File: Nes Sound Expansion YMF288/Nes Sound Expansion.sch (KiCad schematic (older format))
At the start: 44 parts, among them J1 NES-SNES Port1, J2 NES-SNES Port2, J3 EXP 1-24, J4 EXP 25-48, J5 EN Switch, J6 AudioJack2_Ground_Switch, J7 EN LED, U1 74HC139D, U10 74HC257D, U2 74HC132D, U6 74HC174D, U7 74HC174D, U8 74HC257D, U9 74HC257D, X1 CXO_DIP8

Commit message: Added amplification for both famicom and nes model
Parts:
- removed C12, C13: 10uF, Capacitor_SMD:CP_Elec_4x5.3, symbol Device:CP
- removed R1, R2, R3: 1k, Resistor_SMD:R_0805_2012Metric, symbol Device:R
- added C12, C13, C6, C7: 10uF, Capacitor_SMD:C_0805_2012Metric, symbol Device:C
- added C8, C9: 68pF, Capacitor_SMD:C_0805_2012Metric, symbol Device:C
- added R20, R21, R22, R23, R26, R27: 47k, Resistor_SMD:R_0805_2012Metric, symbol Device:R
- added R24, R25: 3k, Resistor_SMD:R_0805_2012Metric, symbol Device:R
- added U3: LM358, Package_SO:SOIC-8_3.9x4.9mm_P1.27mm, symbol Amplifier_Operational:OPA2134
- C2: footprint Capacitor_SMD:CP_Elec_4x5.3 -> Capacitor_SMD:C_0805_2012Metric; symbol Device:CP -> Device:C
- R10: value 1k -> 10k
- X1: footprint Oscillator:Oscillator_SMD_SeikoEpson_SG8002CE-4Pin_3.2x2.5mm -> Oscillator:Oscillator_SMD_SeikoEpson_SG8002LB-4Pin_5.0x3.2mm
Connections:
- wire segments 118 -> 139
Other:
- moved on the sheet: C10, C11, R10, R5, R6, R7, R8, U10, U8, U9

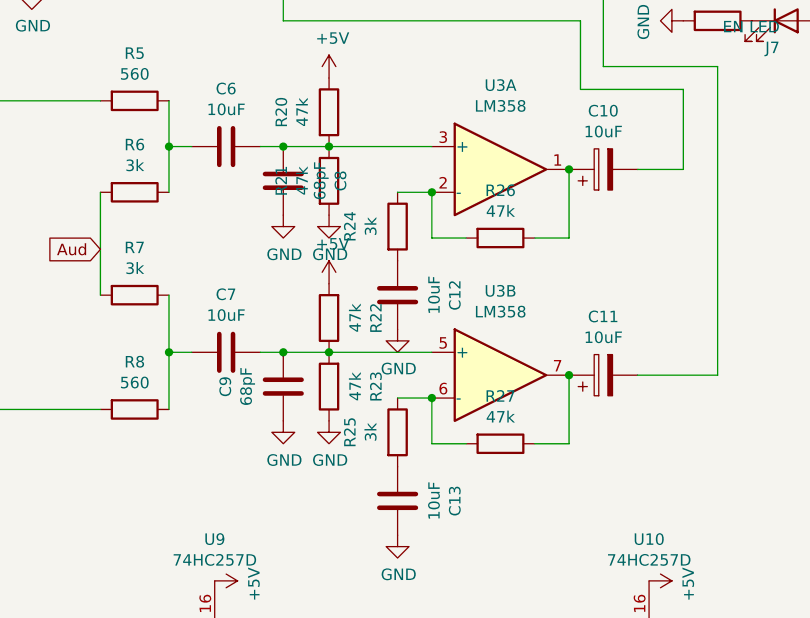
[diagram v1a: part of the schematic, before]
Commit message: Updated 401C-F addressing circuit
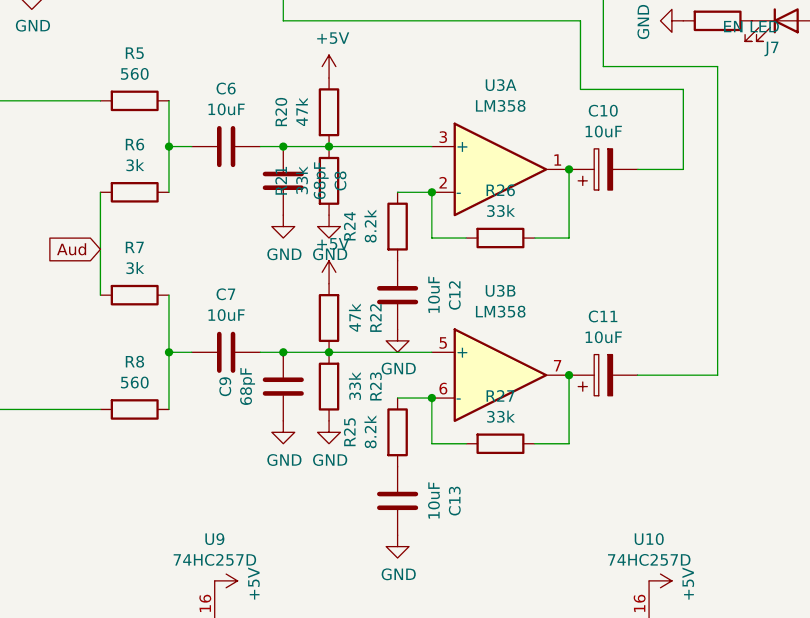
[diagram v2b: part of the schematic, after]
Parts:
- R21, R23, R26, R27: value 47k -> 33k
- R24, R25: value 3k -> 8.2k
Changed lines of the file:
@@
 P 9500 4000
 F 0 "R27" V 9293 4000 50  0000 C CNN
-F 1 "47k" V 9384 4000 50  0000 C CNN
+F 1 "33k" V 9384 4000 50  0000 C CNN
 F 2 "Resistor_SMD:R_0805_2012Metric" V 9430 4000 50  0001 C CNN
 F 3 "~" H 9500 4000 50  0001 C CNN
@@
 P 9050 3950
 F 0 "R25" V 8843 3950 50  0000 C CNN
-F 1 "3k" V 8934 3950 50  0000 C CNN
+F 1 "8.2k" V 8934 3950 50  0000 C CNN
 F 2 "Resistor_SMD:R_0805_2012Metric" V 8980 3950 50  0001 C CNN
 F 3 "~" H 9050 3950 50  0001 C CNN
@@
 P 8750 3750
 F 0 "R23" V 8543 3750 50  0000 C CNN
-F 1 "47k" V 8634 3750 50  0000 C CNN
+F 1 "33k" V 8634 3750 50  0000 C CNN
 F 2 "Resistor_SMD:R_0805_2012Metric" V 8680 3750 50  0001 C CNN
 F 3 "~" H 8750 3750 50  0001 C CNN
@@
 P 9500 3100
 F 0 "R26" V 9293 3100 50  0000 C CNN
-F 1 "47k" V 9384 3100 50  0000 C CNN
+F 1 "33k" V 9384 3100 50  0000 C CNN
 F 2 "Resistor_SMD:R_0805_2012Metric" V 9430 3100 50  0001 C CNN
 F 3 "~" H 9500 3100 50  0001 C CNN
@@
 P 9050 3050
 F 0 "R24" V 8843 3050 50  0000 C CNN
-F 1 "3k" V 8934 3050 50  0000 C CNN
+F 1 "8.2k" V 8934 3050 50  0000 C CNN
 F 2 "Resistor_SMD:R_0805_2012Metric" V 8980 3050 50  0001 C CNN
 F 3 "~" H 9050 3050 50  0001 C CNN
@@
 P 8750 2850
 F 0 "R21" V 8543 2850 50  0000 C CNN
-F 1 "47k" V 8634 2850 50  0000 C CNN
+F 1 "33k" V 8634 2850 50  0000 C CNN
 F 2 "Resistor_SMD:R_0805_2012Metric" V 8680 2850 50  0001 C CNN
 F 3 "~" H 8750 2850 50  0001 C CNN

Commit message: Removed power switch and updated resistor values
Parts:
- removed J5: EN Switch, Button_Switch_SMD:SW_DIP_SPSTx01_Slide_6.7x4.1mm_W6.73mm_P2.54mm_LowProfile_JPin, symbol Switch:SW_SPST
- R13: value 1k -> 3k
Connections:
- wire segments 139 -> 138
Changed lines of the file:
@@
 $EndComp
-Wire Wire Line
-	10600 1850 10500 1850
 Wire Wire Line
 	10500 1850 10500 2050
@@
 P 3600 6050
 F 0 "R13" V 3393 6050 50  0000 C CNN
-F 1 "1k" V 3484 6050 50  0000 C CNN
+F 1 "3k" V 3484 6050 50  0000 C CNN
 F 2 "Resistor_SMD:R_0805_2012Metric" V 3530 6050 50  0001 C CNN
 F 3 "~" H 3600 6050 50  0001 C CNN
@@
 	10500 2050 10900 2050
 $Comp
-L Switch:SW_SPST J5
-U 1 1 5F6BC120
-P 10800 1850
-F 0 "J5" H 10772 1732 50  0000 R CNN
-F 1 "EN Switch" H 10772 1823 50  0000 R CNN
-F 2 "Button_Switch_SMD:SW_DIP_SPSTx01_Slide_6.7x4.1mm_W6.73mm_P2.54mm_LowProfile_JPin" H 10800 1850 50  0001 C CNN
-F 3 "~" H 10800 1850 50  0001 C CNN
-	1    10800 1850
-	-1   0    0    1
-$EndComp
-Wire Wire Line
-	10600 1750 11000 1750
-Wire Wire Line
-	11000 1750 11000 1850
-$Comp
 L Device:C C4
 U 1 1 60444BC0
@@
 	1    0    0    -1
 $EndComp
+Wire Wire Line
+	10600 1750 10500 1750
+Wire Wire Line
+	10500 1750 10500 1850
 $EndSCHEMATC

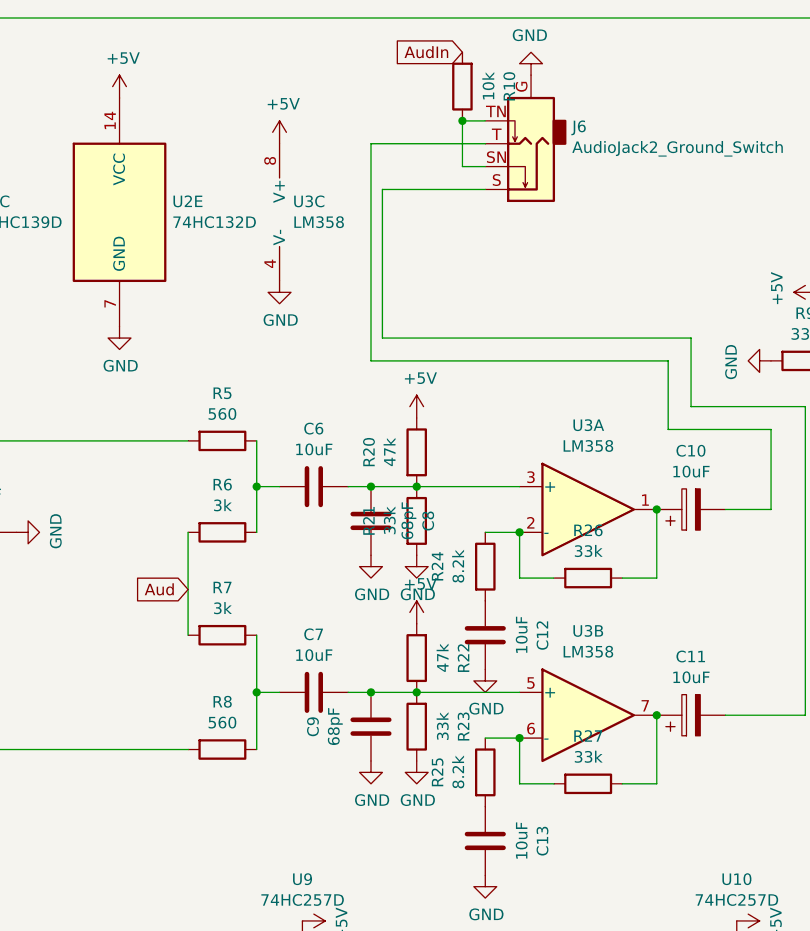
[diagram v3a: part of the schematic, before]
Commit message: Forgot to press save after editing resistor values
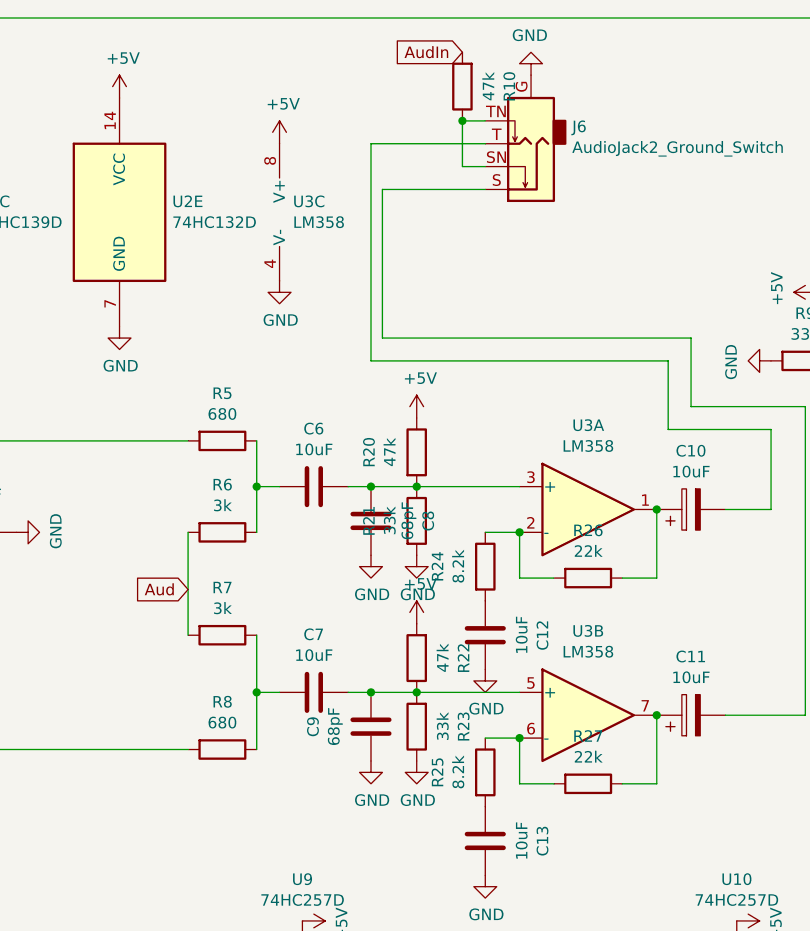
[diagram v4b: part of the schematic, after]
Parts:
- R10: value 10k -> 47k
- R26, R27: value 33k -> 22k
- R5, R8: value 560 -> 680
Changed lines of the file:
@@
 P 7900 2500
 F 0 "R5" V 7693 2500 50  0000 C CNN
-F 1 "560" V 7784 2500 50  0000 C CNN
+F 1 "680" V 7784 2500 50  0000 C CNN
 F 2 "Resistor_SMD:R_0805_2012Metric" V 7830 2500 50  0001 C CNN
 F 3 "~" H 7900 2500 50  0001 C CNN
@@
 P 7900 3850
 F 0 "R8" V 7693 3850 50  0000 C CNN
-F 1 "560" V 7784 3850 50  0000 C CNN
+F 1 "680" V 7784 3850 50  0000 C CNN
 F 2 "Resistor_SMD:R_0805_2012Metric" V 7830 3850 50  0001 C CNN
 F 3 "~" H 7900 3850 50  0001 C CNN
@@
 P 8950 950
 F 0 "R10" V 8743 950 50  0000 C CNN
-F 1 "10k" V 8834 950 50  0000 C CNN
+F 1 "47k" V 8834 950 50  0000 C CNN
 F 2 "Resistor_SMD:R_0805_2012Metric" V 8880 950 50  0001 C CNN
 F 3 "~" H 8950 950 50  0001 C CNN
@@
 P 9500 4000
 F 0 "R27" V 9293 4000 50  0000 C CNN
-F 1 "33k" V 9384 4000 50  0000 C CNN
+F 1 "22k" V 9384 4000 50  0000 C CNN
 F 2 "Resistor_SMD:R_0805_2012Metric" V 9430 4000 50  0001 C CNN
 F 3 "~" H 9500 4000 50  0001 C CNN
@@
 P 9500 3100
 F 0 "R26" V 9293 3100 50  0000 C CNN
-F 1 "33k" V 9384 3100 50  0000 C CNN
+F 1 "22k" V 9384 3100 50  0000 C CNN
 F 2 "Resistor_SMD:R_0805_2012Metric" V 9430 3100 50  0001 C CNN
 F 3 "~" H 9500 3100 50  0001 C CNN
